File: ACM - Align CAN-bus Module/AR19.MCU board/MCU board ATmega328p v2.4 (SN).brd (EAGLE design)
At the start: 34 x 25 mm, 50 parts, among them IC1 ATMEGA328P-MMH, IC2 MIC5239-5.0YS_TR, IC3 MCP25625-E_ML, J1 AVR_SPI_PROG_3X2NS, U1 CSTNE16M0V530000R0, U2 CSTNE16M0V530000R0

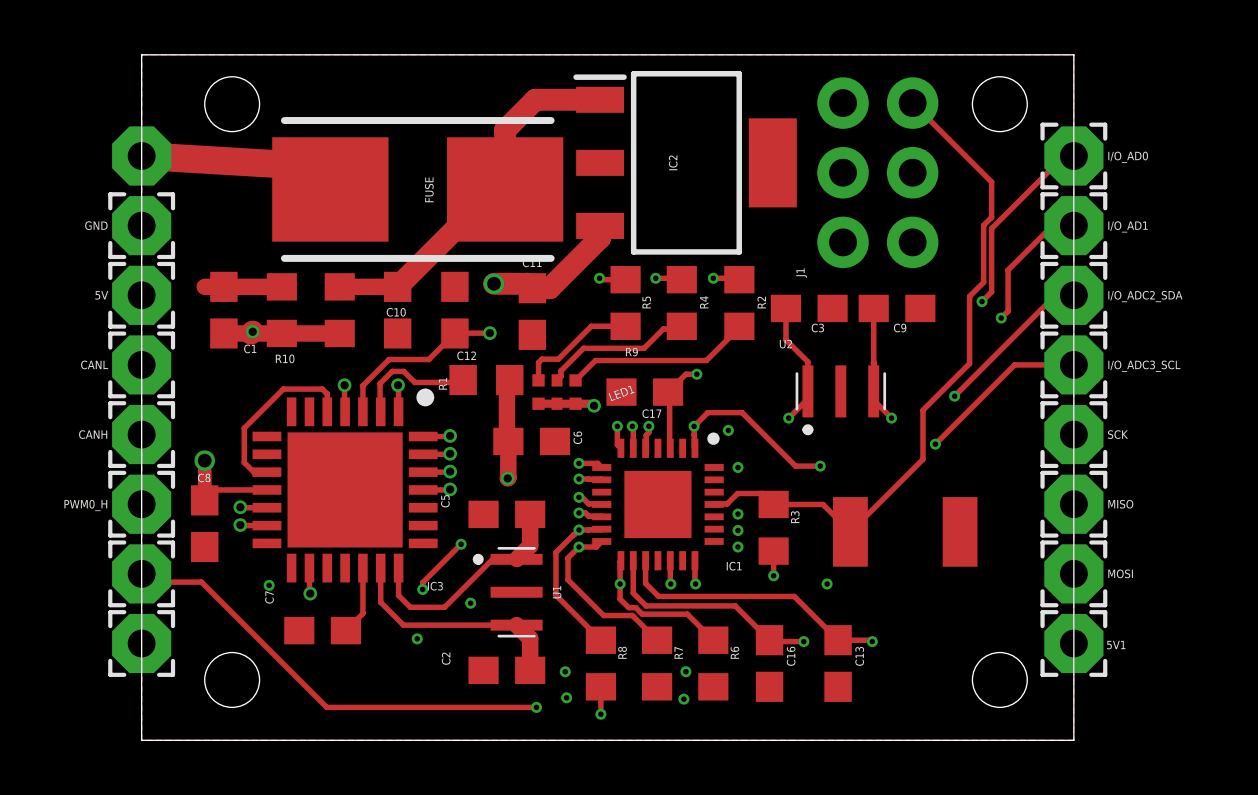
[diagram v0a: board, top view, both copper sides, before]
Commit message: Removed all errors, except dimension errors.
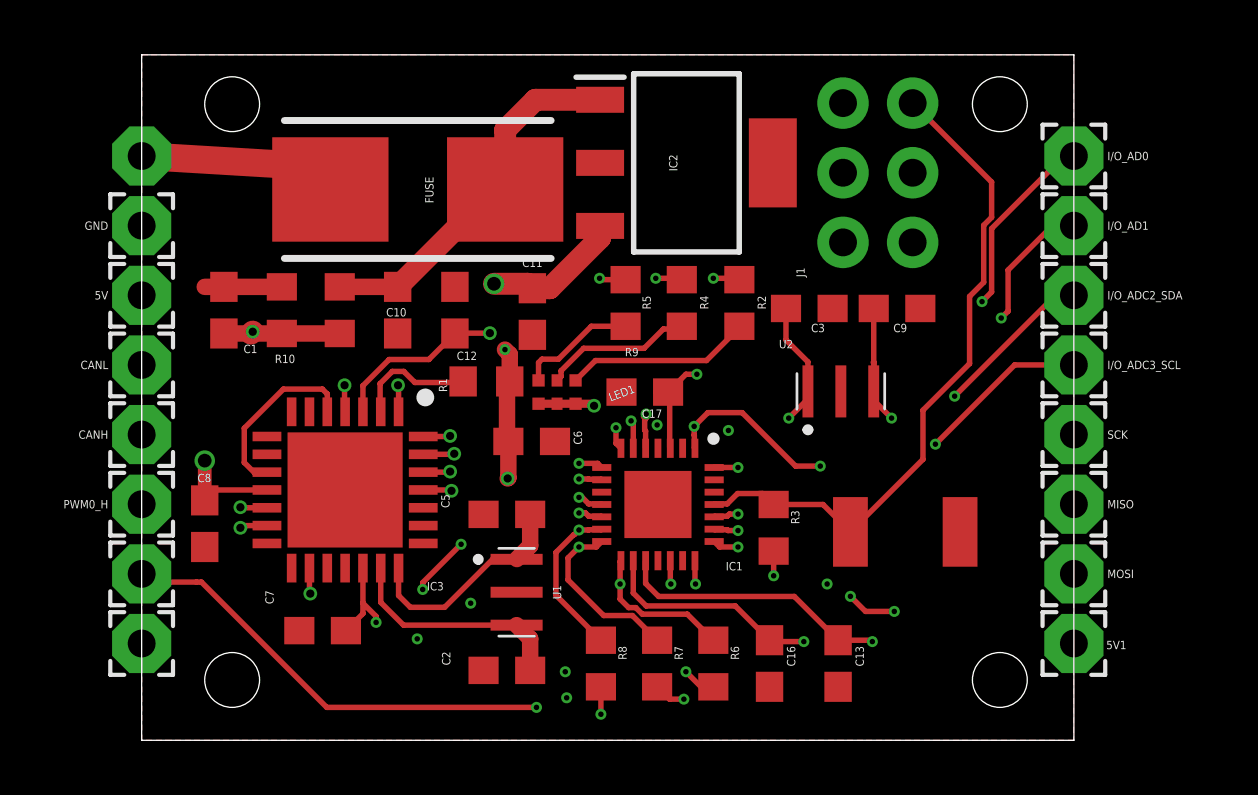
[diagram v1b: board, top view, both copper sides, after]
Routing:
- net N$2: track 24.5 -> 30.7 mm, vias 2 -> 1
- net 5V: track 47.1 -> 51.0 mm, vias 9 -> 13
- net N$10: track 17.4 -> 19.0 mm
- net N$11: track 16.8 -> 18.3 mm
- net I/OADC2: track 16.5 -> 17.8 mm
- net I/O_ADC3: track 14.2 -> 15.4 mm
- net I/OAD0: track 22.6 -> 23.5 mm
- net CAN_INT: track 19.4 -> 20.2 mm
- net GND: vias 0 -> 1
